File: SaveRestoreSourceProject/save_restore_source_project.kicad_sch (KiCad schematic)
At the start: 4 parts

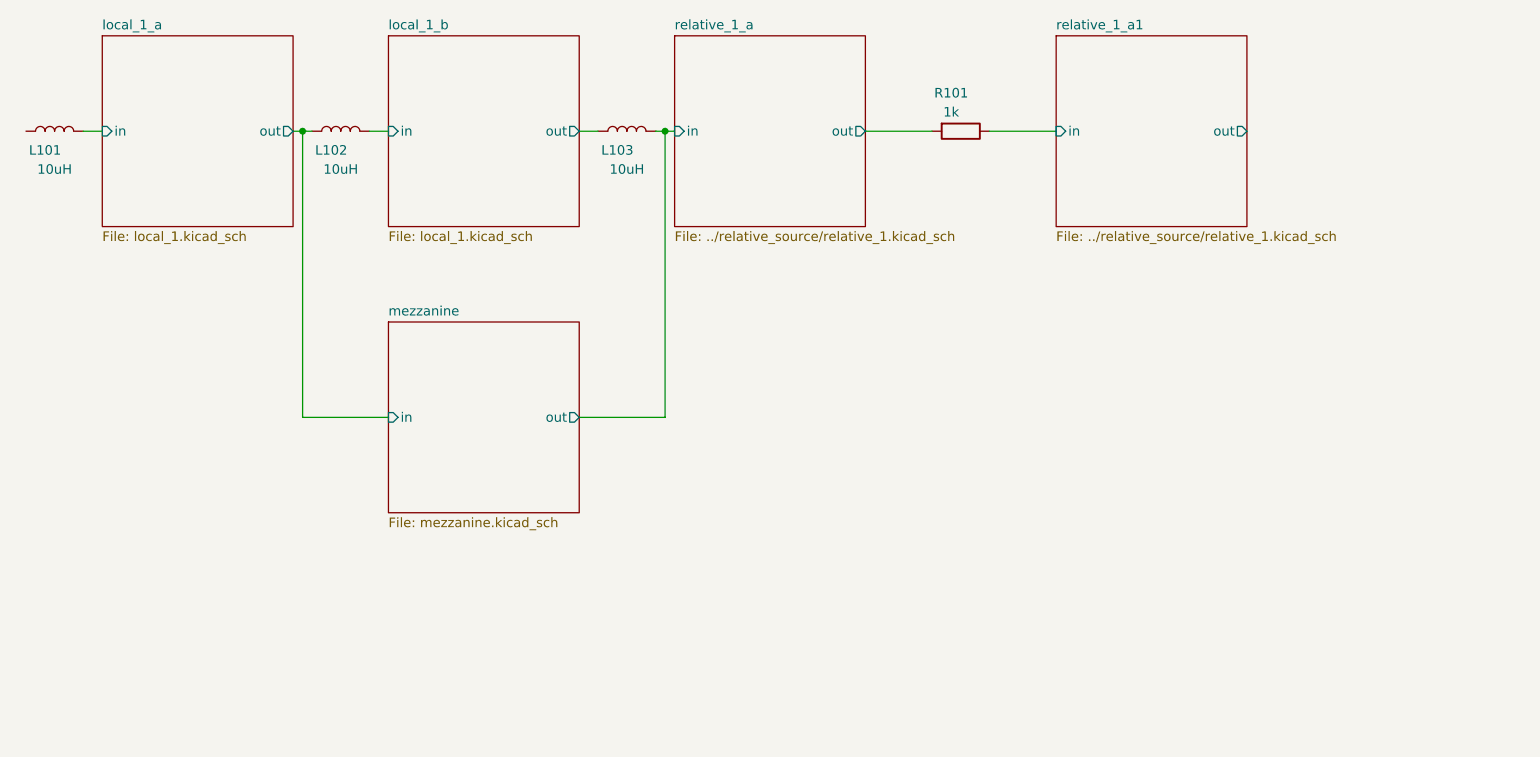
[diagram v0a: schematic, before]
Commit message: Add support for connected drawings, update test template
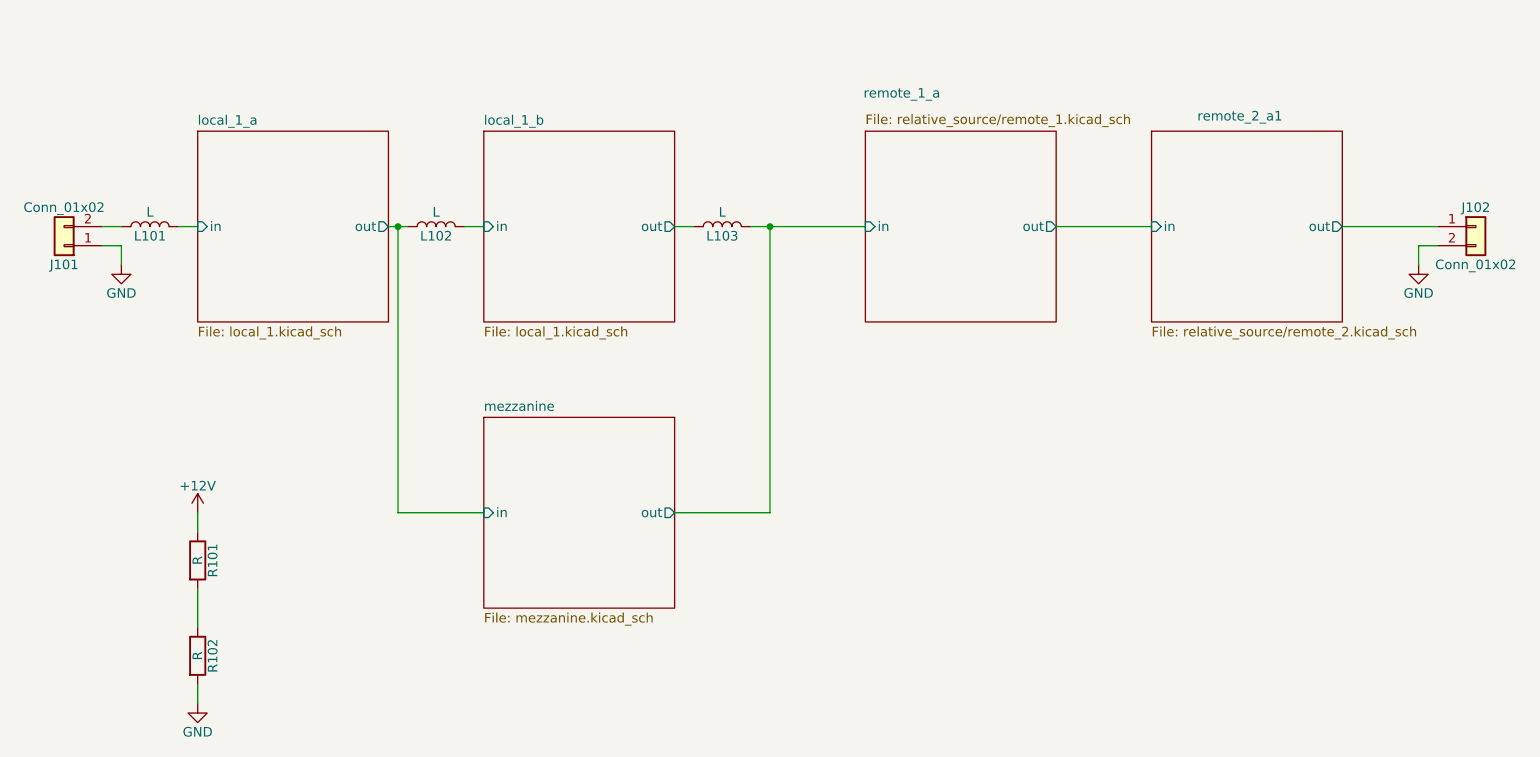
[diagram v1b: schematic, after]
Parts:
- added J101, J102: Conn_01x02, Connector_PinHeader_2.54mm:PinHeader_1x02_P2.54mm_Vertical, symbol Connector_Generic:Conn_01x02
- added R102: R, Resistor_SMD:R_1206_3216Metric, symbol Device:R
- L101, L102, L103: value 10uH -> L; footprint Inductor_SMD:L_1206_3216Metric_Pad1.22x1.90mm_HandSolder -> Inductor_SMD:L_1206_3216Metric
- R101: value 1k -> R
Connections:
- net at L101.1: now also J101.2 (Pin_2)
- net relative_1_a/out: no longer names the net of R101.2
- net relative_1_a/out: now also R102.1
- net relative_1_a1/in renamed +12V
- new net GND: J101.1 (Pin_1), J102.2 (Pin_2), R102.2
- new net remote_2_a1/out: J102.1 (Pin_1)
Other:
- removed sheet relative_1_a
- removed sheet relative_1_a1
- added sheet remote_1_a (relative_source/remote_1.kicad_sch)
- added sheet remote_2_a1 (relative_source/remote_2.kicad_sch)
